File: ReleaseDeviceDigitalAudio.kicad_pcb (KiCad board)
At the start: 2 copper layers, 132 x 68.5 mm, 183 parts, among them J1 AudioJack3, J10 UIBoardCON2, J11 KeySwitch, J2 AudioJack3, J3 AudioJack3, J4 AudioJack3, J5 AudioJack3, J6 ATMEGA_PROG, J7 SignalStrength, J8 UIBoardCON1, J9 Conn_01x03, Q1 BSS314PEH6327XTSA1, Q3 SQ2362ES-T1_GE3, Q4 SQD50P06-15L_GE3, U1 ATmega4809-A, U10 ULN2003F12FN-7, U11 ULN2003F12FN-7, U12 ULN2003F12FN-7, U13 ULN2003F12FN-7, U14 MAX98089ETN+, U15 SN74LV1T126, U16 SN74LV1T126, U17 BM83SM1-00TA, U18 PCF85063A, U2 VOMA617A, U3 VOMA617A, U4 LM53635LQRNL*Q1, U5 TLVH431AQDBVRQ1, U6 LM74610-Q1, U7 Compute_Module_4_Connectors, U8 CD4514BM, U9 CD4511BPWR, Y1 9HT12

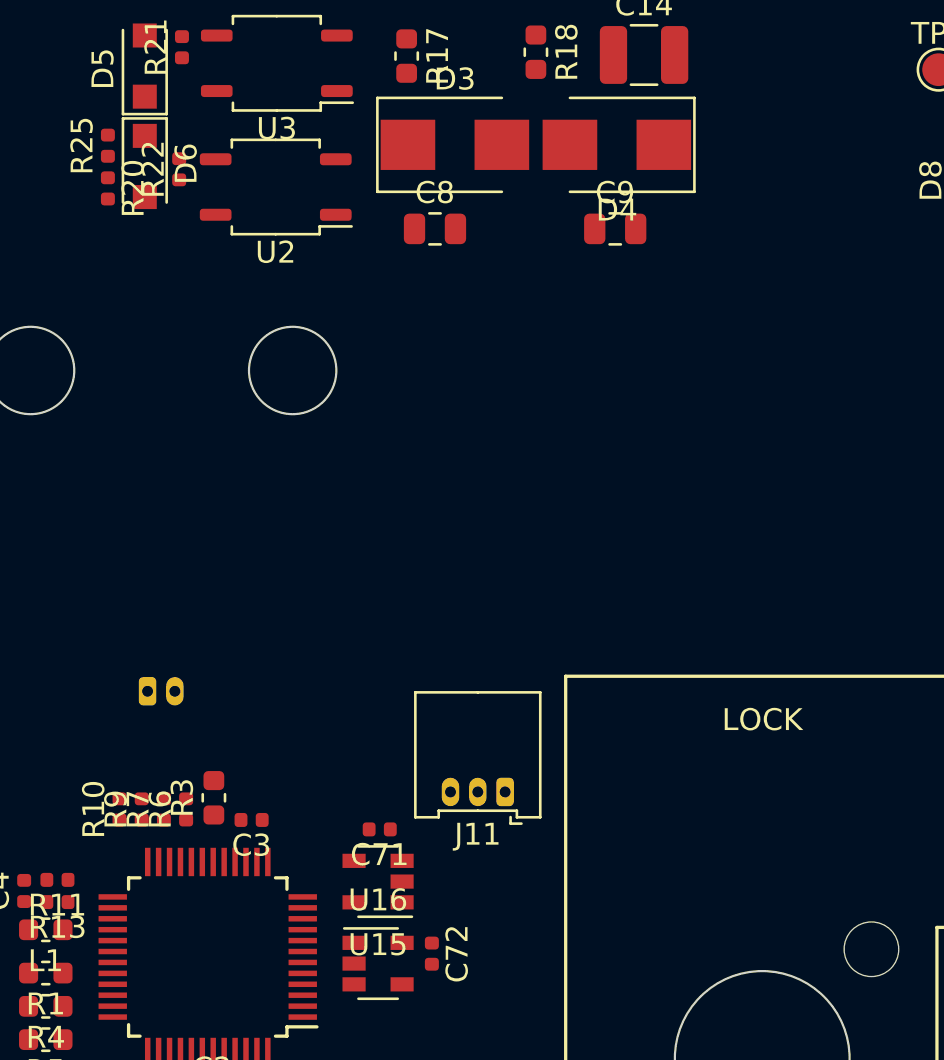
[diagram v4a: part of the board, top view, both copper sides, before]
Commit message: - Board auf 4 Lagen umgestellt, GND und 5V Lagen eingefügt
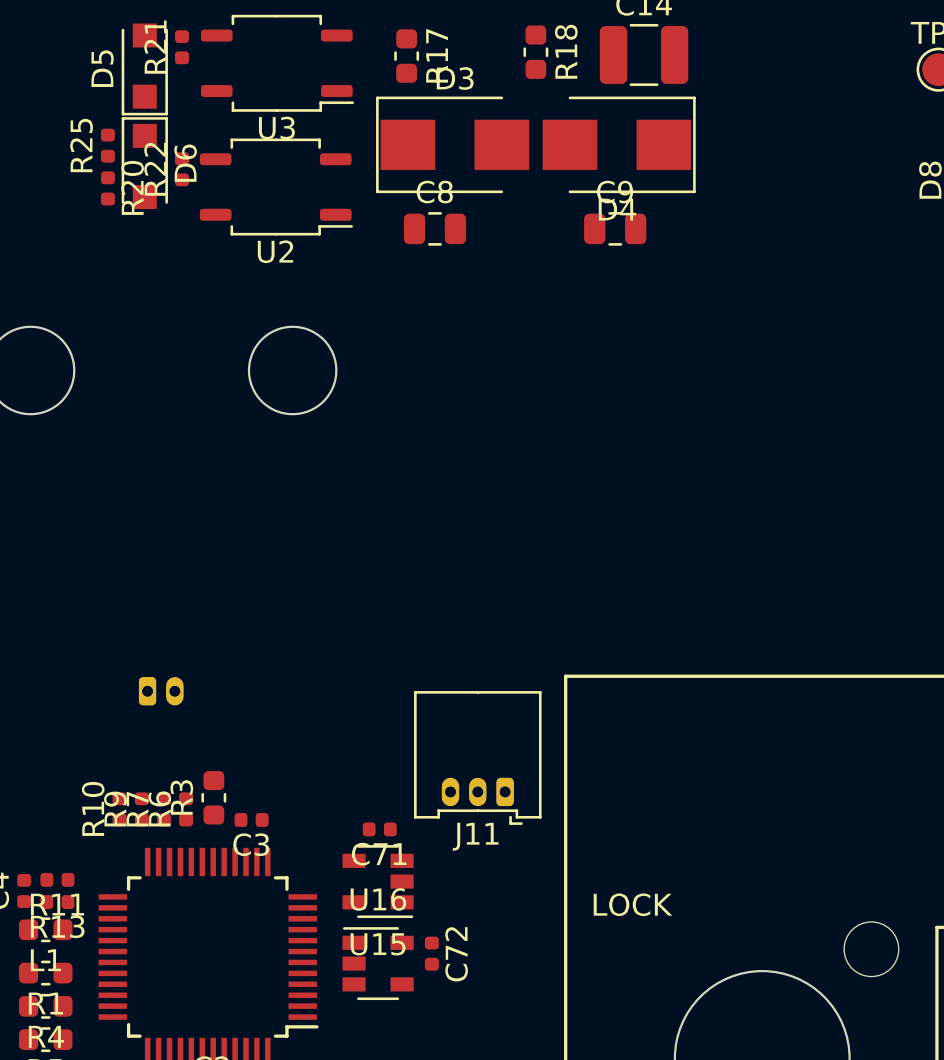
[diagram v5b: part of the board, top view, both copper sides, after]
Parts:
- moved R22 0.13 mm to (103.4, 81.8)
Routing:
- added copper zone on In2.Cu, net +5V
- added copper zone on In1.Cu, net GND
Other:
- copper layers 2 -> 4
- net class Default: clearance 0.2 -> 0.1524; trace_width 0.25 -> 0.2032; via_dia 0.8 -> 0.6096; via_drill 0.4 -> 0.3048
- net class Power Low added: clearance 0.2032, trace_width 0.254, via_dia 0.6096, via_drill 0.3048
- rule trace_clearance: 0.2 -> 0.1524
- rule trace_min: 0.2 -> 0.1524
- rule via_min_drill: 0.3 -> 0.254
- rule via_min_size: 0.4 -> 0.3048
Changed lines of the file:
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@@
   (layers
     (0 F.Cu signal)
+    (1 In1.Cu power)
+    (2 In2.Cu power hide)
     (31 B.Cu signal)
     (32 B.Adhes user)
@@
     (46 B.CrtYd user)
     (47 F.CrtYd user)
-    (48 B.Fab user)
+    (48 B.Fab user hide)
     (49 F.Fab user hide)
   )
   (setup
-    (last_trace_width 0.25)
-    (user_trace_width 0.5)
-    (user_trace_width 0.75)
-    (trace_clearance 0.2)
-    (zone_clearance 0.508)
+    (last_trace_width 0.2032)
+    (user_trace_width 0.2032)
+    (user_trace_width 0.254)
+    (user_trace_width 0.4064)
+    (user_trace_width 0.762)
+    (trace_clearance 0.1524)
+    (zone_clearance 0.4064)
     (zone_45_only no)
-    (trace_min 0.2)
-    (via_size 0.8)
-    (via_drill 0.4)
-    (via_min_size 0.4)
-    (via_min_drill 0.3)
-    (uvia_size 0.3)
-    (uvia_drill 0.1)
+    (trace_min 0.1524)
+    (via_size 0.6096)
+    (via_drill 0.3048)
+    (via_min_size 0.3048)
+    (via_min_drill 0.254)
+    (user_via 0.6096 0.3048)
+    (uvia_size 0.3048)
+    (uvia_drill 0.1524)
     (uvias_allowed no)
     (uvia_min_size 0.2)
@@
   (net 354 "Net-(U18-Pad1)")
   (net_class Default "This is the default net class."
-    (clearance 0.2)
-    (trace_width 0.25)
-    (via_dia 0.8)
-    (via_drill 0.4)
-    (uvia_dia 0.3)
-    (uvia_drill 0.1)
-    (add_net +1V8)
-    (add_net +3V3)
-    (add_net +5V)
+    (clearance 0.1524)
+    (trace_width 0.2032)
+    (via_dia 0.6096)
+    (via_drill 0.3048)
+    (uvia_dia 0.3048)
+    (uvia_drill 0.1524)
     (add_net +BATT)
     (add_net -BATT)
@@
     (add_net /RPiCM4/WL_nDisable)
     (add_net /RPiCM4/nRPIBOOT)
-    (add_net GND)
     (add_net "Net-(BT1-Pad1)")
     (add_net "Net-(C16-Pad2)")
@@
     (add_net VPP)
   )
+  (net_class "Power Low" ""
+    (clearance 0.2032)
+    (trace_width 0.254)
+    (via_dia 0.6096)
+    (via_drill 0.3048)
+    (uvia_dia 0.3048)
+    (uvia_drill 0.1524)
+    (add_net +1V8)
+    (add_net +3V3)
+    (add_net +5V)
+    (add_net GND)
+  )
   (module Connector_PinHeader_2.54mm:PinHeader_1x03_P2.54mm_Horizontal (layer F.Cu)
     (at 114.7975 125.4868 270)
@@
   )
   (module Resistor_SMD:R_0402_1005Metric (layer F.Cu)
-    (at 103.304 81.7861 90)
+    (at 103.431 81.7861 90)
     (descr "Resistor SMD 0402 (1005 Metric), square (rectangular) end terminal, IPC_7351 nominal, (Body size source: http://www.tortai-tech.com/upload/download/2011102023233369053.pdf), generated with kicad-footprint-generator")
     (tags resistor)
@@
   (gr_circle (center 96.5 91) (end 98.5 91) (layer Edge.Cuts) (width 0.1))
   (gr_circle (center 130 122.5) (end 134 122.5) (layer Edge.Cuts) (width 0.1))
-  (gr_text LOCK (at 130 107) (layer F.SilkS)
+  (gr_text LOCK (at 124 115.5) (layer F.SilkS)
     (effects (font (size 1 1) (thickness 0.15)))
   )
@@
     (polygon
       (pts
-        (xy 139.5 116.5) (xy 138 116.5) (xy 138 129.5) (xy 121 129.5) (xy 121 105)
-        (xy 139.5 105)
+        (xy 139.5 116.5) (xy 138 116.5) (xy 138 129.5) (xy 121 129.5) (xy 121 113.5)
+        (xy 139.5 113.5)
+      )
+    )
+  )
+  (zone (net 2) (net_name GND) (layer In1.Cu) (hatch edge 0.508)
+    (connect_pads (clearance 0.4064))
+    (min_thickness 0.1524)
+    (fill yes (arc_segments 32) (thermal_gap 0.254) (thermal_bridge_width 1.016))
+    (polygon
+      (pts
+        (xy 216 129.5) (xy 84 129.5) (xy 84 61) (xy 216 61)
+      )
+    )
+  )
+  (zone (net 1) (net_name +5V) (layer In2.Cu) (hatch edge 0.508)
+    (connect_pads (clearance 0.4064))
+    (min_thickness 0.1524)
+    (fill yes (arc_segments 32) (thermal_gap 0.254) (thermal_bridge_width 1.016))
+    (polygon
+      (pts
+        (xy 216 129.5) (xy 84 129.5) (xy 84 61) (xy 216 61)
       )
     )

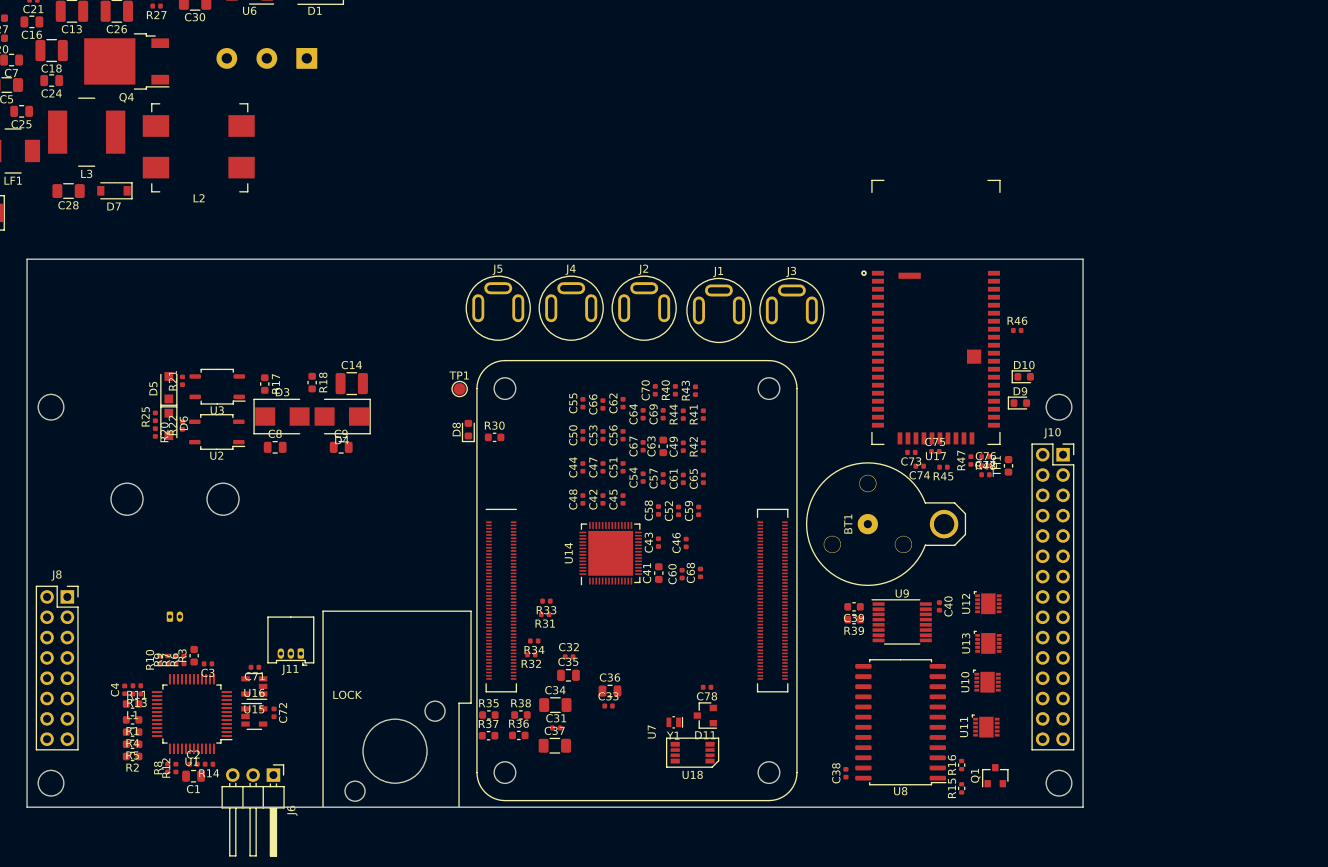
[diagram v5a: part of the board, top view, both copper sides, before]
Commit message: - neue Stecker hinzugefügt, Annotation überall entsprechend angepasst Footprint fehlt noch
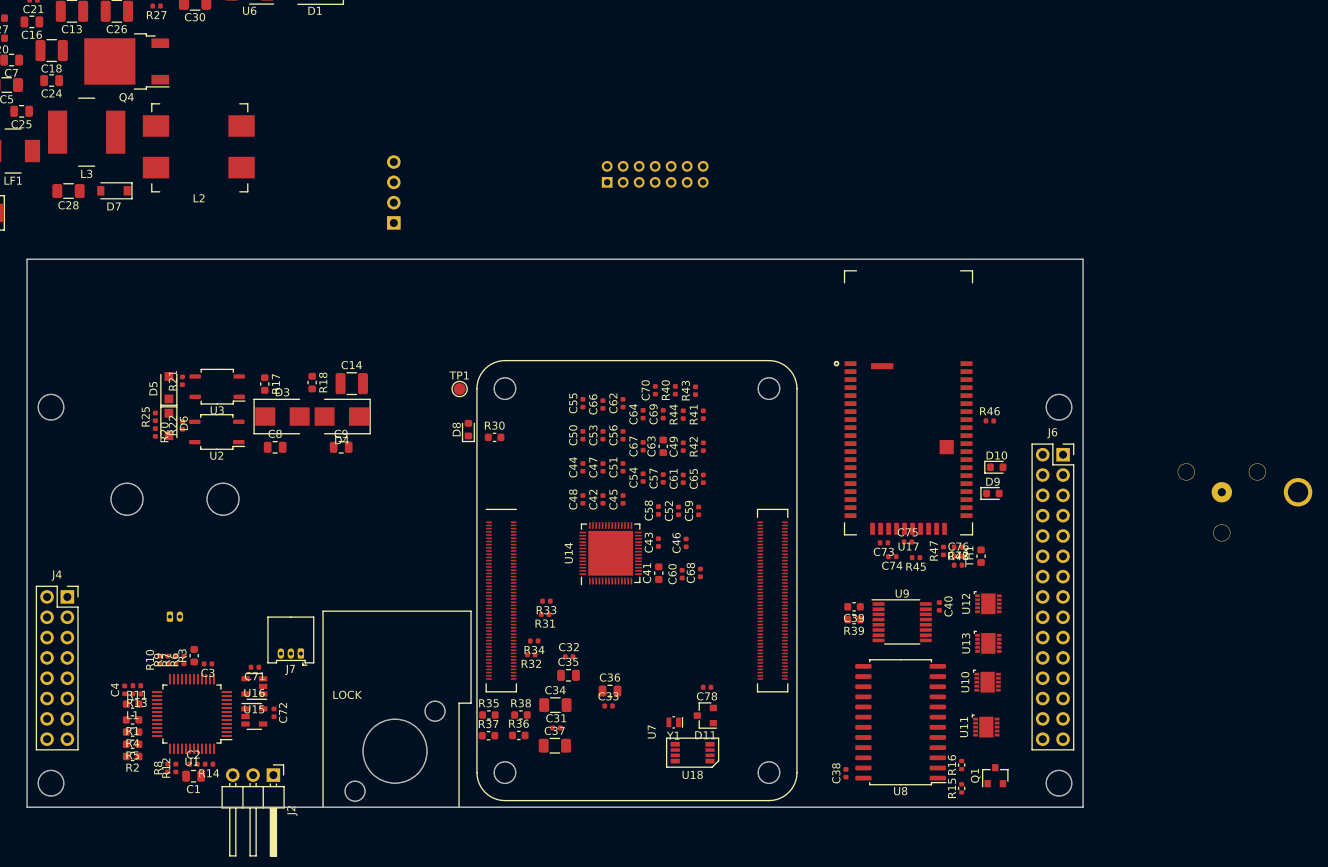
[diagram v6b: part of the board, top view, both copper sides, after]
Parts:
- removed the J2 at (161.1, 67.1)
- removed the J3 at (179.6, 67.4)
- removed the J4 at (152.0, 67.1)
- removed J9: Conn_01x03, TerminalBlock_Phoenix:TerminalBlock_Phoenix_MKDS-1,5-3_1x03_P5.00mm_Horizontal
- BT1: moved to B.Cu
- J1: value AudioJack3 -> Conn_02x08_Counter_Clockwise; footprint TeKaDe:LumbergKLB4 -> Connector_PinSocket_2.00mm:PinSocket_2x07_P2.00mm_Vertical; moved to B.Cu
- J5: value AudioJack3 -> Conn_01x04; footprint TeKaDe:LumbergKLB4 -> Connector_PinSocket_2.54mm:PinSocket_1x04_P2.54mm_Vertical; moved to B.Cu
- moved BT1 44.4 mm to (242.9, 90.1)
- moved J1 21.3 mm to (156.5, 51.4), turned to 270 degrees
- moved J5 16.9 mm to (129.8, 56.5)
- moved R45 11.8 mm to (195.1, 98.3)
- moved R47 11.8 mm to (198.6, 97.5)
- moved C73 11.8 mm to (191.1, 96.5)
- moved C74 11.8 mm to (192.2, 98.2)
- moved C75 11.8 mm to (194.1, 96.4)
- moved C77 11.8 mm to (200.4, 99.2)
- moved D10 11.8 mm to (205.2, 87.0)
- moved D9 11.8 mm to (204.7, 90.3)
- moved R46 11.8 mm to (204.3, 81.2)
- moved R48 11.8 mm to (200.4, 97.0)
- moved TH1 11.8 mm to (203.3, 98.1)
- moved U17 11.8 mm to (194.2, 79.0)
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- renumbered J6 to J2, J7 to J3, J8 to J4, J10 to J6, J11 to J7

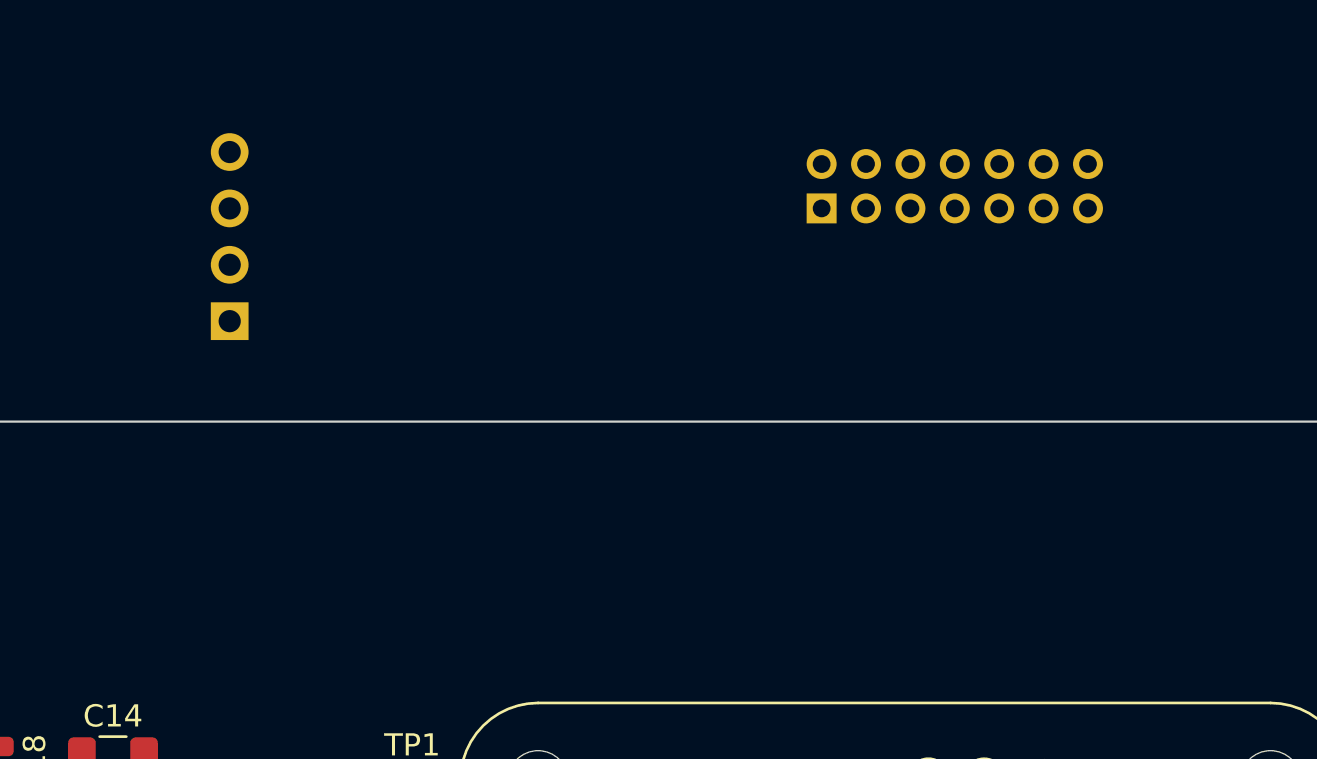
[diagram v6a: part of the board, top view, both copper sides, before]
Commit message: - Footprints inkl. 3D model aller Steckverbinder fertig
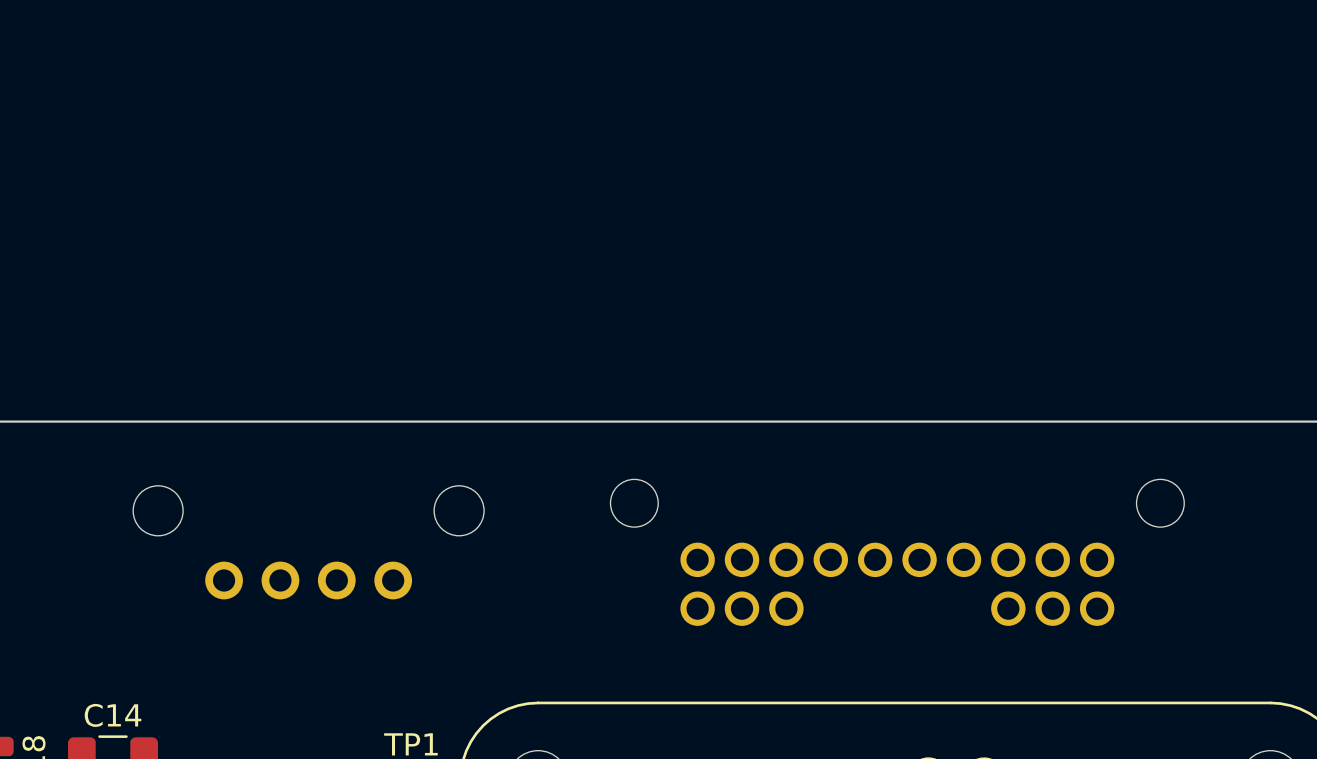
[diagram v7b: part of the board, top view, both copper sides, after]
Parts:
- J1: footprint Connector_PinSocket_2.00mm:PinSocket_2x07_P2.00mm_Vertical -> TeKaDe:Molex_34825-0160
- J3: footprint Connector_Molex:Molex_PicoBlade_53048-0210_1x02_P1.25mm_Horizontal -> TeKaDe:Molex_PicoBlade_53048-0210_1x02_P1.25mm_Horizontal
- J5: footprint Connector_PinSocket_2.54mm:PinSocket_1x04_P2.54mm_Vertical -> TeKaDe:Molex_31101-0040
- J7: footprint Connector_Molex:Molex_PicoBlade_53048-0310_1x03_P1.25mm_Horizontal -> TeKaDe:Molex_PicoBlade_53048-0310_1x03_P1.25mm_Horizontal
- moved J1 18.9 mm to (150.9, 69.4), turned to 0 degrees
- moved J5 11.7 mm to (129.6, 68.2)
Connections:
- J1 pad 11: /MasterMicInN -> /HeadsetMicInN
- J1 pad 12: GND -> /HeadsetMicInP
- J1 pad 13: /Line_In_R -> GND
- J1 pad 14: /Audio_Handset_Out_R -> /Line_In_R
- J1 pad 7: GND -> /Audio_Master_Out_R
- J1 pad 8: /HeadsetMicInP -> GND
- J1 pad 9: /HeadsetMicInN -> /Audio_Handset_Out_R
